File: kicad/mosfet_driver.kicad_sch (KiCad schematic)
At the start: 55 parts, among them U21 LP2981-50DBVR, U23 74LVC2T45DC,125, U23 OPA4191xRUMx, U24 74LVC2T45DC,125, U26 MAX5719AGSD+

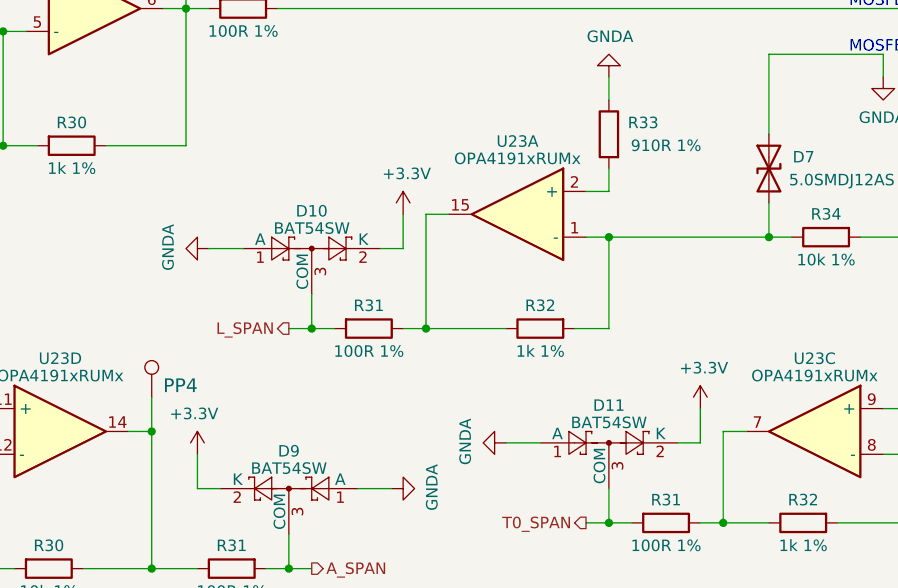
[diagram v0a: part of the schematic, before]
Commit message: bugfix: driver for 4th T, capacitors for input amps
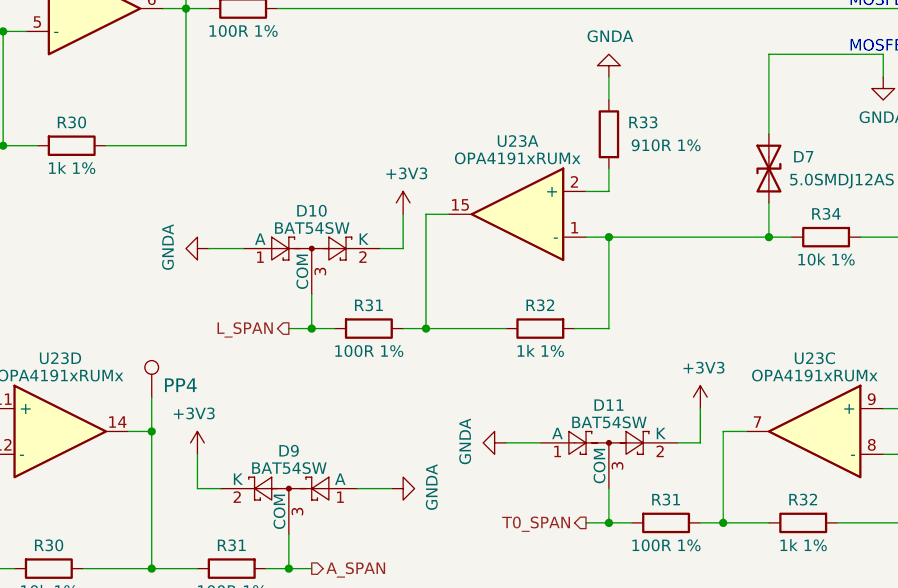
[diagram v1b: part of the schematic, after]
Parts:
- C70: value GCM31CR71C106KA64L -> GCM31CR71C106KA64L
- U23, U24: value 74LVC2T45DC,125 -> 74LVC2T45DC,125
